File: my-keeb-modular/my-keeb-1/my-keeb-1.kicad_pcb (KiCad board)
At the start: 2 copper layers, 190.5 x 95.2 mm, 94 parts, among them SW1 SW_Push, U1 ProMicro

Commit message: Working on part2 pcb
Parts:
- removed D24, D25, D26, D27, D28, D29, D30, D31, D32, D33, D34, D35, D36, D37, D38, D39, D40, D41, D42, D43, D44, D45, D46: SOD-123, Keebio-Parts:Diode-Hybrid-Back
- removed MX24, MX25, MX26, MX27, MX29, MX30, MX31, MX32, MX33, MX34, MX35, MX36, MX37, MX38, MX39, MX40, MX41, MX42, MX43, MX44, MX45, MX46: MX-NoLED, MX_Alps_Hybrid:MX-1U-NoLED
- removed MX28: MX-NoLED, MX_Alps_Hybrid:MX-1.5U-NoLED
- added M1: 1x5, modular:1x5, F.Cu at (107.1, 59.7)
- added M2: 1x5, modular:1x5, F.Cu at (107.2, 78.6)
- added M3: 1x5, modular:1x5, F.Cu at (107.1, 41.8)
- moved U1 76.2 mm to (41.3, 31.0)
- moved SW1 63.5 mm to (25.4, 31.8)
- moved D19 11.2 mm to (98.4, 30.2), turned to 180 degrees
- moved D2 11.2 mm to (22.2, 49.2), turned to 180 degrees
- moved D21 11.2 mm to (98.4, 68.3), turned to 180 degrees
- moved D22 11.2 mm to (98.4, 87.3), turned to 180 degrees
- moved D5 11.2 mm to (41.3, 30.2), turned to 180 degrees
- moved D6 11.2 mm to (41.3, 49.2), turned to 180 degrees
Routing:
- net ROW3: track 215.0 -> 90.4 mm
- net ROW2: track 193.2 -> 102.5 mm
- net COL4: track 92.1 -> 176.1 mm
- net ROW1: track 180.6 -> 101.4 mm
- net ROW0: track 174.8 -> 103.3 mm
- net COL9: track 130.2 -> 62.2 mm
- net COL3: track 118.8 -> 166.9 mm
- net COL8: track 106.8 -> 62.4 mm
- net COL7: track 108.4 -> 68.8 mm
- net Net-(SW1-Pad1): track 42.2 -> 13.6 mm
- net GND: track 64.3 -> 42.6 mm
- net COL2: track 137.6 -> 158.3 mm
- net COL0: track 153.4 -> 170.1 mm
- net ROW4: track 179.1 -> 163.0 mm
- net Net-(D25-Pad2): track 13.3 -> 0.00 mm
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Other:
- board size 190.5 x 95.2 mm -> 95.2 x 95.2 mm

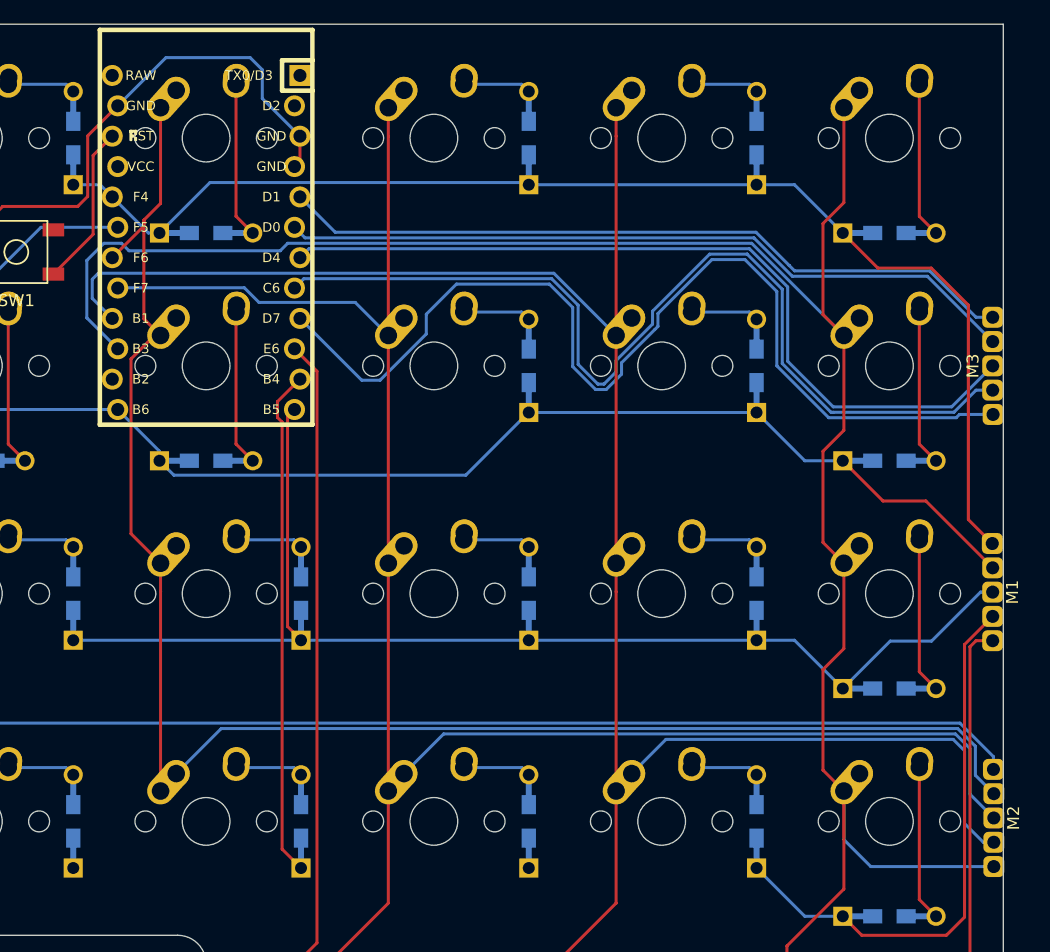
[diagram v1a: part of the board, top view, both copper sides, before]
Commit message: Fixed track issues
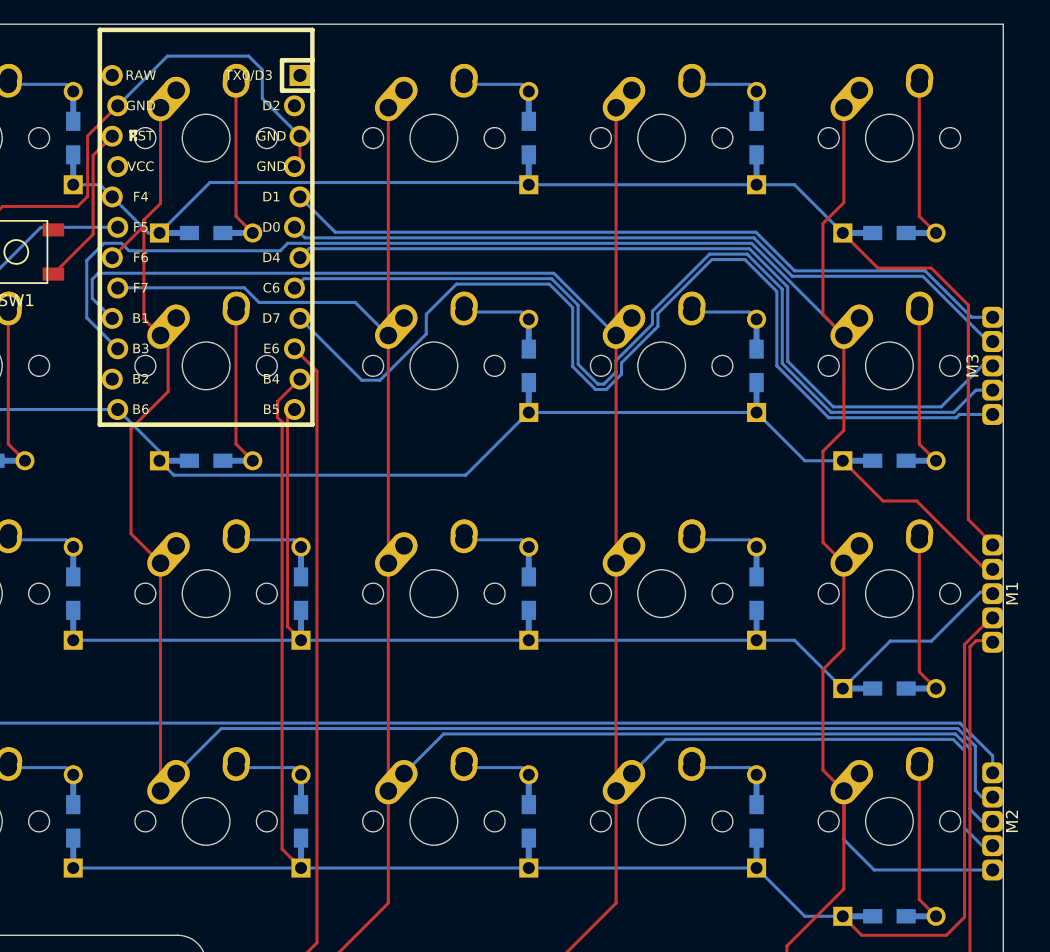
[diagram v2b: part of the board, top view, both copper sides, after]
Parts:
- moved M2 0.30 mm to (107.1, 78.9)
- moved M1 0.13 mm to (107.1, 59.8)
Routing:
- net ROW3: track 90.4 -> 147.5 mm
- net COL1: track 139.0 -> 140.5 mm
- net COL2: track 158.3 -> 159.0 mm
